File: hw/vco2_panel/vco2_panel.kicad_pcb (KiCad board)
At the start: 2 copper layers, 60.6 x 128.5 mm, 1 part

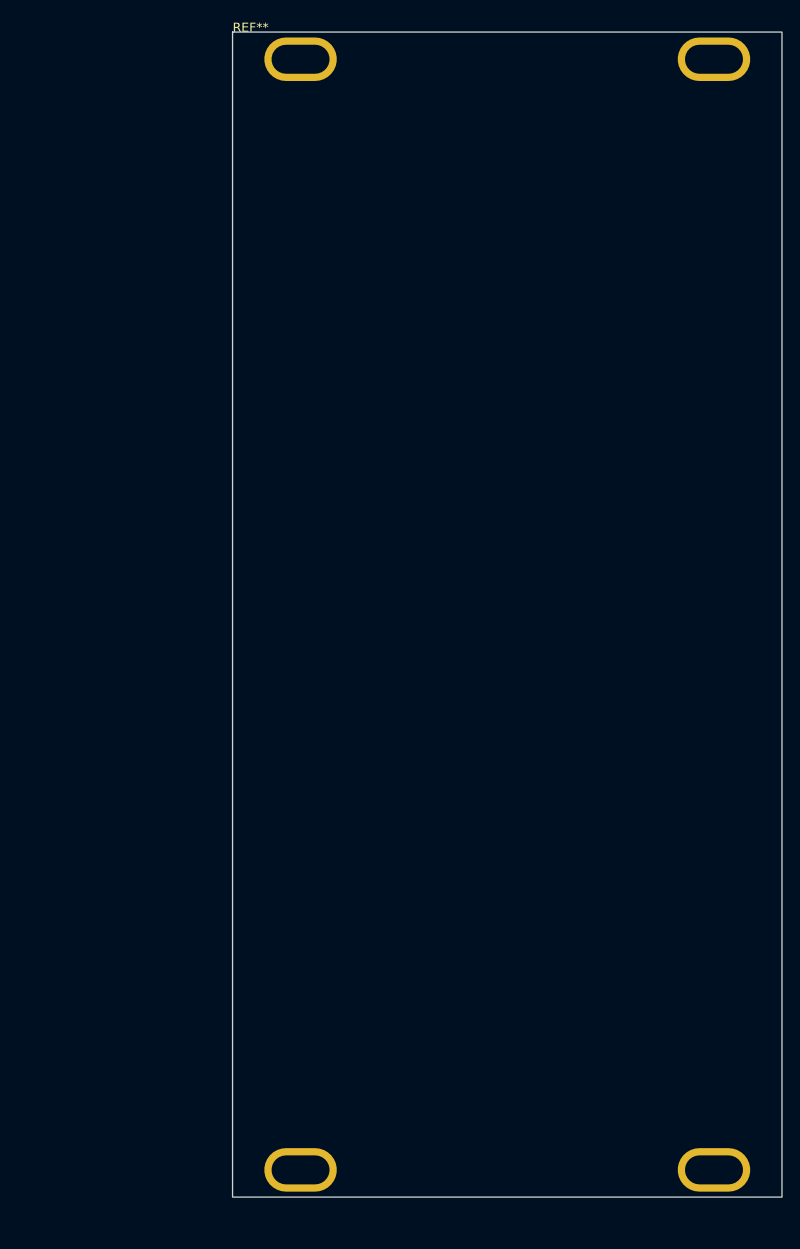
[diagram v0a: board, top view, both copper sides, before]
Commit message: Blank panel for VCO2
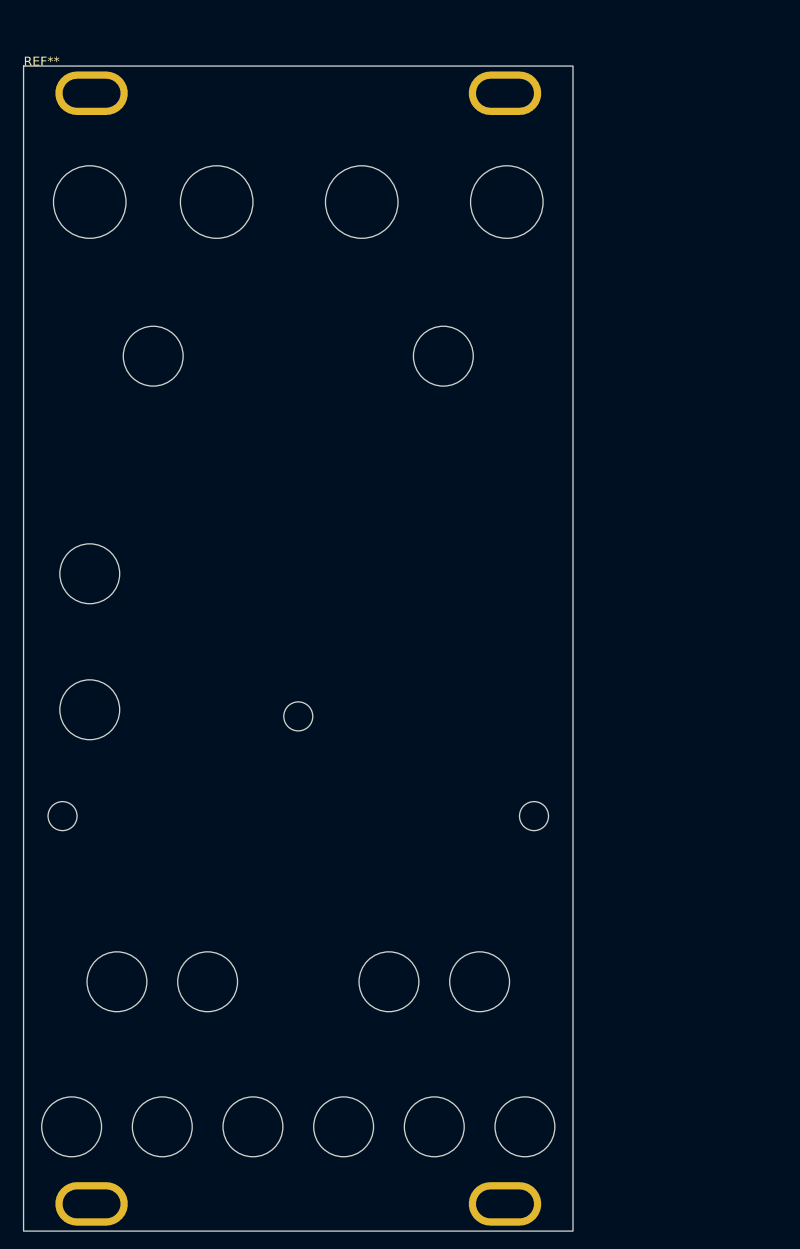
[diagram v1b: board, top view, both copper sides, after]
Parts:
- added G***: LOGO, elemental:elemental-25.4mm, B.Cu at (111.0, 37.0)
- added REF**: Pot hole M7 shaft, Eurorack:Pot hole M7 shaft, F.Cu at (87.0, 46.0)
- added REF**: Pot hole 6mm shaft, Eurorack:Pot hole 6mm shaft, F.Cu at (85.0, 148.0)
- added REF**: Pot hole M7 shaft, Eurorack:Pot hole M7 shaft, F.Cu at (101.0, 46.0)
- added REF**: Pot hole M7 shaft, Eurorack:Pot hole M7 shaft, F.Cu at (117.0, 46.0)
- added REF**: Pot hole 6mm shaft, Eurorack:Pot hole 6mm shaft, F.Cu at (105.0, 148.0)
- added REF**: Pot hole M7 shaft, Eurorack:Pot hole M7 shaft, F.Cu at (133.0, 46.0)
- added REF**: Pot hole 6mm shaft, Eurorack:Pot hole 6mm shaft, F.Cu at (87.0, 102.0)
- added REF**: Pot hole 6mm shaft, Eurorack:Pot hole 6mm shaft, F.Cu at (90.0, 132.0)
- added REF**: Led 3mm hole, Eurorack:Led 3mm hole, F.Cu at (84.0, 115.0)
- added REF**: Pot hole 6mm shaft, Eurorack:Pot hole 6mm shaft, F.Cu at (94.0, 63.0)
- added REF**: Led 3mm hole, Eurorack:Led 3mm hole, F.Cu at (136.0, 115.0)
- added REF**: Pot hole 6mm shaft, Eurorack:Pot hole 6mm shaft, F.Cu at (95.0, 148.0)
- added REF**: Pot hole 6mm shaft, Eurorack:Pot hole 6mm shaft, F.Cu at (87.0, 87.0)
- added REF**: Led 3mm hole, Eurorack:Led 3mm hole, F.Cu at (110.0, 104.0)
- added REF**: Pot hole 6mm shaft, Eurorack:Pot hole 6mm shaft, F.Cu at (126.0, 63.0)
- added REF**: Pot hole 6mm shaft, Eurorack:Pot hole 6mm shaft, F.Cu at (100.0, 132.0)
- added REF**: Pot hole 6mm shaft, Eurorack:Pot hole 6mm shaft, F.Cu at (115.0, 148.0)
- added REF**: Pot hole 6mm shaft, Eurorack:Pot hole 6mm shaft, F.Cu at (120.0, 132.0)
- added REF**: Pot hole 6mm shaft, Eurorack:Pot hole 6mm shaft, F.Cu at (130.0, 132.0)
- added REF**: Pot hole 6mm shaft, Eurorack:Pot hole 6mm shaft, F.Cu at (135.0, 148.0)
- added REF**: Pot hole 6mm shaft, Eurorack:Pot hole 6mm shaft, F.Cu at (125.0, 148.0)
- moved REF** 23.4 mm to (79.7, 31.0)

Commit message: VCO2 panel
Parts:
- added G***: LOGO, LOGO, F.Cu at (109.8, 95.5)
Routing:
- added copper zone on B.Cu, net (none)
- added copper zone on F.Cu, net (none)

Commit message: Update VCO2 panel
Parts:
- added G***: LOGO, elemental:elemental-4mm, F.Cu at (120.4, 156.2)
- moved G*** 0.54 mm to (110.2, 95.2)

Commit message: WIP: VCO2 panel
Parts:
- removed the G*** at (110.2, 95.2)
- removed the REF** at (84.0, 115.0)
- removed the REF** at (136.0, 115.0)
- removed the REF** at (110.0, 104.0)
- added G***: LOGO, LOGO, F.Cu at (110.0, 95.2)
- added G***: LOGO, LOGO, F.Cu at (110.0, 95.0)
- moved REF** 16.0 mm to (88.0, 62.0)
- moved REF** 16.0 mm to (132.0, 62.0)
- moved REF** 12.7 mm to (103.0, 72.0)
- moved REF** 12.7 mm to (117.0, 72.0)
- moved REF** 6.00 mm to (105.0, 142.0)
- moved REF** 6.00 mm to (90.0, 126.0)
- moved REF** 6.00 mm to (95.0, 142.0)
- moved REF** 6.00 mm to (100.0, 126.0)
- moved REF** 6.00 mm to (115.0, 142.0)
- moved REF** 6.00 mm to (120.0, 126.0)
- moved REF** 6.00 mm to (130.0, 126.0)
- moved REF** 6.00 mm to (135.0, 142.0)
- moved REF** 6.00 mm to (125.0, 142.0)
- moved REF** 6.00 mm to (85.0, 142.0)
- moved REF** 2.00 mm to (119.0, 46.0)
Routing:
- removed copper zone on B.Cu, net (none)
- removed copper zone on F.Cu, net (none)

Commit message: VCO2 production work
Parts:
- removed the G*** at (120.4, 156.2)
- added REF**: Pot hole 6mm shaft, Eurorack:Pot hole 6mm shaft, F.Cu at (134.0, 92.5)

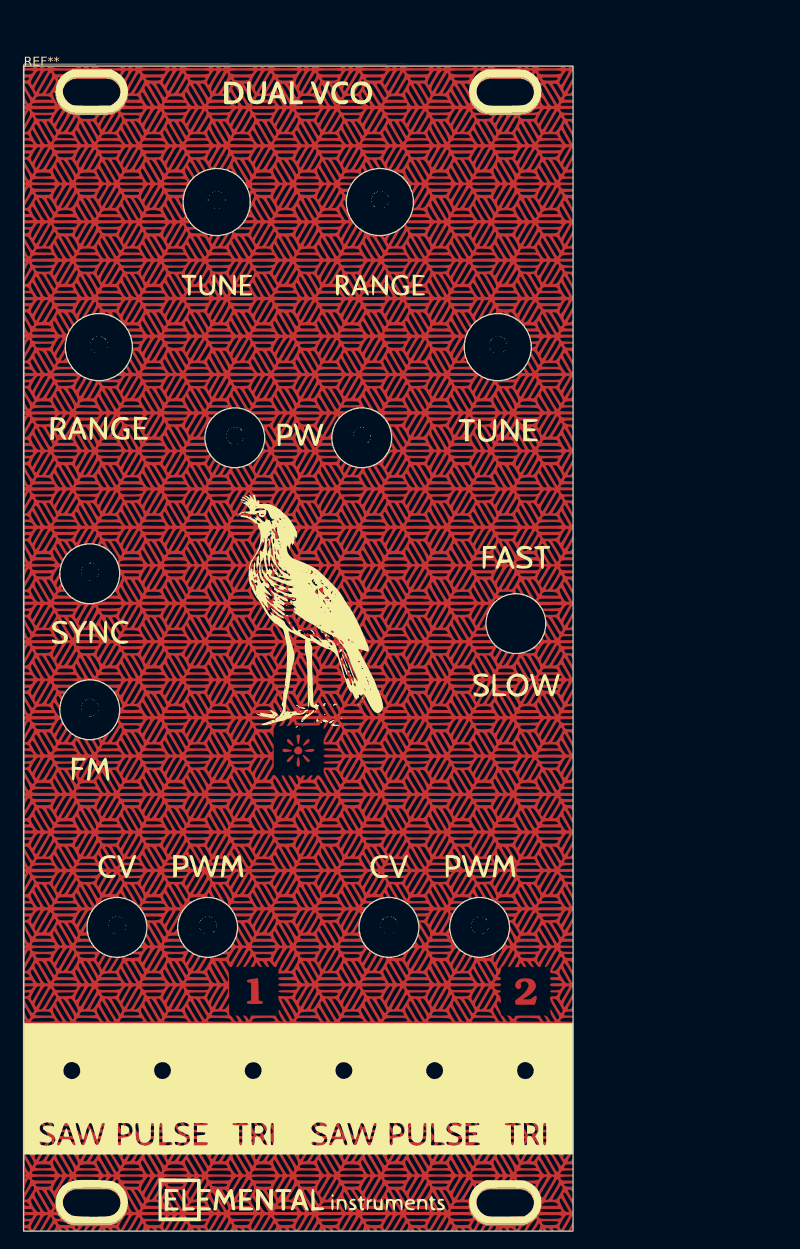
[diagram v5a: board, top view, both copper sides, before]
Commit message: VCO2 rev 2 as sent for production at JLCPCB
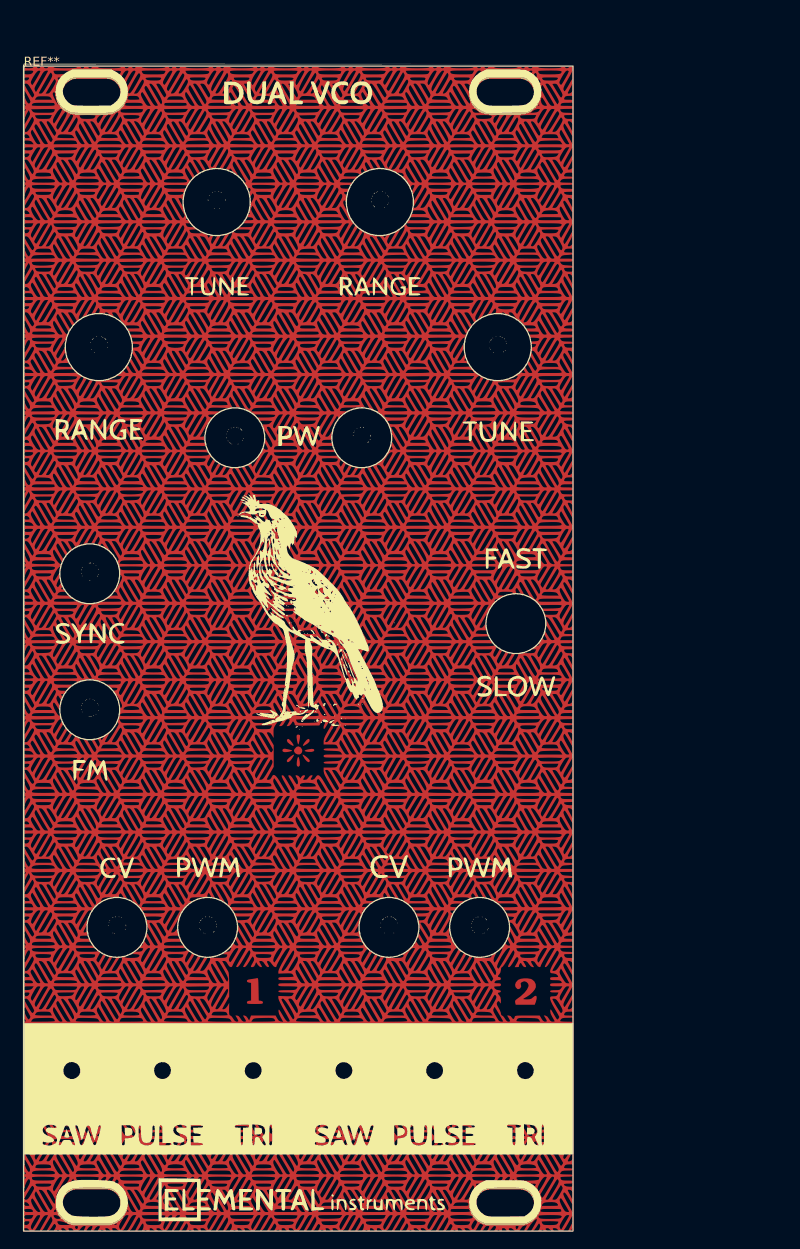
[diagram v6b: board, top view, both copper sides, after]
